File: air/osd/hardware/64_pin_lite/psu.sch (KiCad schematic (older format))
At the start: 22 parts, among them U4 BD9G101G, U5 LD39015MXXR

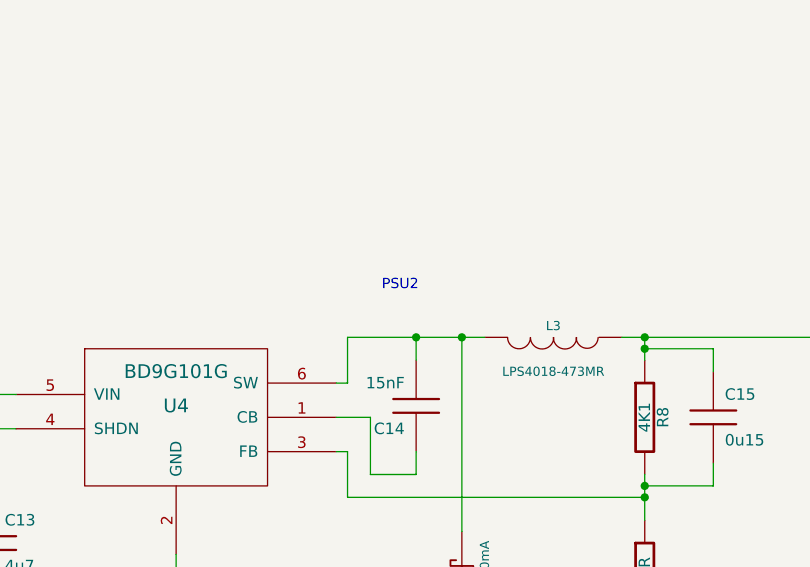
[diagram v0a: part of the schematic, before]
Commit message: No functional changes,just tidying up air osd schematic project
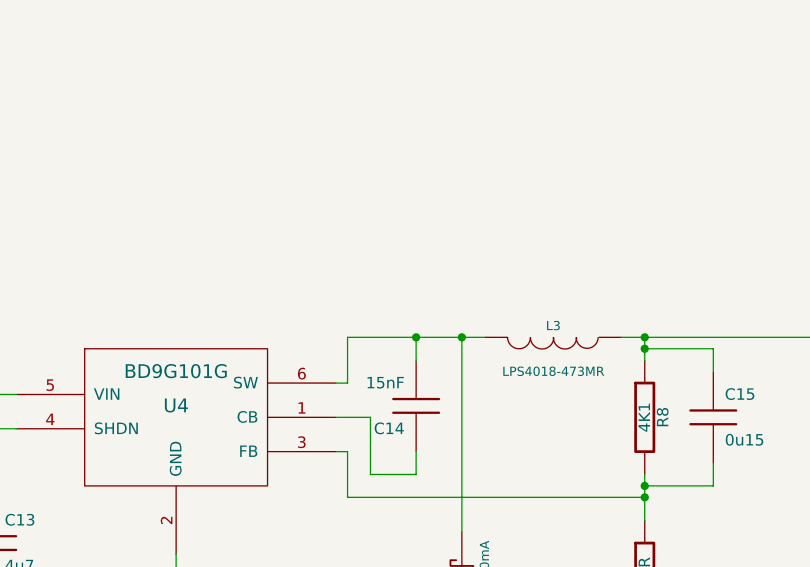
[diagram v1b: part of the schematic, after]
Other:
- note removed: "PSU2"
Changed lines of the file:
@@
-EESchema Schematic File Version 2  date Mon 26 Jan 2015 12:08:39 GMT
+EESchema Schematic File Version 2  date Mon 26 Jan 2015 12:32:55 GMT
 LIBS:lm358
 LIBS:conn_6
@@
 Sheet 3 8
 Title "noname.sch"
-Date "21 jan 2015"
+Date "26 jan 2015"
 Rev ""
 Comp ""
@@
 	0    1    1    0
 $EndComp
-Text Notes 4250 3000 0    45   ~ 0
-PSU2
 $Comp
 L INDUCTOR L3

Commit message: removed traces on pcb design. Added links to separate ground paths for modules. Moved mpu to other side of board. Added 2 pin power conector at end of board
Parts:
- added LK1, LK10, LK11, LK12, LK13, LK14, LK2, LK3, LK4, LK5, LK6, LK7, LK8, LK9: LINK, symbol LINK
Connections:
- net labels added: HUB_+3.3V, SWITCHER_+5V, SWITCHER_FB, SWITCHER_OUT, SWITCHER_VIN, VIN+RECT, VIN-
- wire segments 79 -> 120
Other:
- moved on the sheet: C12, C16, C17, C18, C19, C20, D3, D6, L4, R10

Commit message: laid out components on boar. No traces done yet
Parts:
- removed LK1, LK10, LK11, LK12, LK13, LK14, LK2, LK3, LK4, LK5, LK6, LK7, LK8, LK9: LINK, symbol LINK
- added C42: 0u1, 0603, symbol C
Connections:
- net labels added: BLUE_LED_RES, SWITCHER_CB
- wire segments 120 -> 141
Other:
- moved on the sheet: C12, C17

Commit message: started routing v2 board, having done component placement
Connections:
- wire segments 141 -> 90
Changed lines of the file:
@@
-EESchema Schematic File Version 2  date Thu 05 Mar 2015 23:13:03 GMT
+EESchema Schematic File Version 2  date Fri 06 Mar 2015 00:28:55 GMT
 LIBS:lm358
 LIBS:conn_6
@@
 Sheet 3 8
 Title "noname.sch"
-Date "5 mar 2015"
+Date "6 mar 2015"
 Rev ""
 Comp ""
@@
 	1500 4050 1500 4300
 Wire Wire Line
-	1500 4300 1100 4300
-Wire Wire Line
-	1100 4300 900  4300
+	1500 4300 900  4300
 Connection ~ 900  4300
 Wire Wire Line
@@
 	1000 3450 950  3450
 Wire Wire Line
-	950  3450 950  3700
-Wire Wire Line
-	950  3700 950  3850
+	950  3450 950  3850
 Wire Wire Line
 	950  3850 850  3850
@@
 	8100 4600 8100 4400
 Wire Wire Line
-	9500 6450 9100 6450
-Wire Wire Line
-	9100 6450 8950 6450
-Wire Wire Line
-	8950 6450 8800 6450
-Wire Wire Line
-	8800 6450 8650 6450
-Wire Wire Line
-	8650 6450 8500 6450
-Wire Wire Line
-	8500 6450 7300 6450
-Wire Wire Line
-	7300 6450 4300 6450
+	9500 6450 4300 6450
 Connection ~ 8500 6450
 Connection ~ 8650 6450
@@
 Connection ~ 5400 3200
 Wire Wire Line
-	5400 3200 5400 3250
-Wire Wire Line
-	5400 3250 5400 3300
-Wire Wire Line
-	5400 3800 5400 3850
-Wire Wire Line
-	5400 3850 5400 3900
-Wire Wire Line
-	5400 3900 5400 4000
+	5400 3200 5400 3300
+Wire Wire Line
+	5400 3800 5400 4000
 Wire Wire Line
 	5400 4600 5400 4500
@@
 	4100 3400 4100 3200
 Wire Wire Line
-	4100 3200 4400 3200
-Wire Wire Line
-	4400 3200 4600 3200
-Wire Wire Line
-	4600 3200 4700 3200
+	4100 3200 4700 3200
 Wire Wire Line
 	4050 3550 4200 3550
@@
 	4400 3800 4400 3700
 Wire Wire Line
-	6100 3200 6000 3200
-Wire Wire Line
-	6000 3200 5400 3200
-Wire Wire Line
-	5400 3200 5300 3200
-Wire Wire Line
-	6700 3200 6800 3200
-Wire Wire Line
-	6800 3200 6850 3200
-Wire Wire Line
-	6850 3200 7000 3200
-Wire Wire Line
-	2550 3450 2550 3600
-Wire Wire Line
-	2550 3600 2550 3700
-Wire Wire Line
-	2550 3700 2550 3900
+	6100 3200 5300 3200
+Wire Wire Line
+	6700 3200 7000 3200
+Wire Wire Line
+	2550 3450 2550 3900
 Connection ~ 2550 3450
 Wire Wire Line
-	1600 3450 1550 3450
-Wire Wire Line
-	1550 3450 1500 3450
-Wire Wire Line
-	1500 3450 1400 3450
-Wire Wire Line
-	2200 3450 2300 3450
-Wire Wire Line
-	2300 3450 2550 3450
-Wire Wire Line
-	2550 3450 2650 3450
-Wire Wire Line
-	6800 4050 6800 3550
-Wire Wire Line
-	6800 3550 6800 3500
-Wire Wire Line
-	6800 3500 6800 3450
-Wire Wire Line
-	6800 3450 6800 3400
-Wire Wire Line
-	6800 3400 6800 3300
-Wire Wire Line
-	6800 3300 6800 3250
-Wire Wire Line
-	6800 3250 6800 3200
+	1600 3450 1400 3450
+Wire Wire Line
+	2200 3450 2650 3450
+Wire Wire Line
+	6800 4050 6800 3200
 Connection ~ 6800 3200
 Wire Wire Line
@@
 Connection ~ 8800 4600
 Wire Wire Line
-	7300 3800 7400 3800
-Wire Wire Line
-	7400 3800 7500 3800
+	7300 3800 7500 3800
 Wire Wire Line
 	2250 4600 2250 4300
 Connection ~ 2250 4600
 Wire Wire Line
-	2550 3700 2250 3700
-Wire Wire Line
-	2250 3700 1900 3700
+	2550 3700 1900 3700
 Wire Wire Line
 	1900 3700 1900 3900
 Connection ~ 2250 3700
 Wire Wire Line
-	9200 4000 9200 3600
-Wire Wire Line
-	9200 3600 9200 3400
-Wire Wire Line
-	9200 3400 9200 3300
-Wire Wire Line
-	9200 3300 9200 3200
-Wire Wire Line
-	9200 3200 9200 3000
+	9200 4000 9200 3000
 Wire Wire Line
 	9200 3000 10700 3000
@@
 Connection ~ 9200 3400
 Wire Wire Line
-	8800 4000 8800 3800
-Wire Wire Line
-	8800 3800 8800 3300
+	8800 4000 8800 3300
 Wire Wire Line
 	8800 3300 9200 3300
 Connection ~ 9200 3300
 Wire Wire Line
-	9200 4600 8800 4600
-Wire Wire Line
-	8800 4600 8100 4600
-Wire Wire Line
-	8100 4600 7200 4600
-Wire Wire Line
-	7200 4600 6800 4600
-Wire Wire Line
-	6800 4600 6450 4600
-Wire Wire Line
-	6450 4600 6000 4600
-Wire Wire Line
-	6000 4600 5400 4600
-Wire Wire Line
-	5400 4600 4600 4600
-Wire Wire Line
-	4600 4600 4300 4600
-Wire Wire Line
-	4300 4600 3350 4600
-Wire Wire Line
-	3350 4600 2550 4600
-Wire Wire Line
-	2550 4600 2250 4600
-Wire Wire Line
-	2250 4600 1900 4600
-Wire Wire Line
-	1900 4600 950  4600
+	9200 4600 900  4600
 Wire Wire Line
 	850  4050 900  4050
 Wire Wire Line
-	900  4050 900  4300
-Wire Wire Line
-	900  4300 900  4600
-Wire Wire Line
-	900  4600 950  4600
+	900  4050 900  4600
 Wire Wire Line
 	1550 3450 1550 3200
